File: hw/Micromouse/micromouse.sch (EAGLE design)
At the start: 57 parts, among them IC1 DSPIC33FJ64MC804-PT, IC2 DRV8833PWR, J1 GP2Y0A51SK0F, J2 GP2Y0A51SK0F, J3 GP2Y0A41SK0F, SW1 B3F-1000

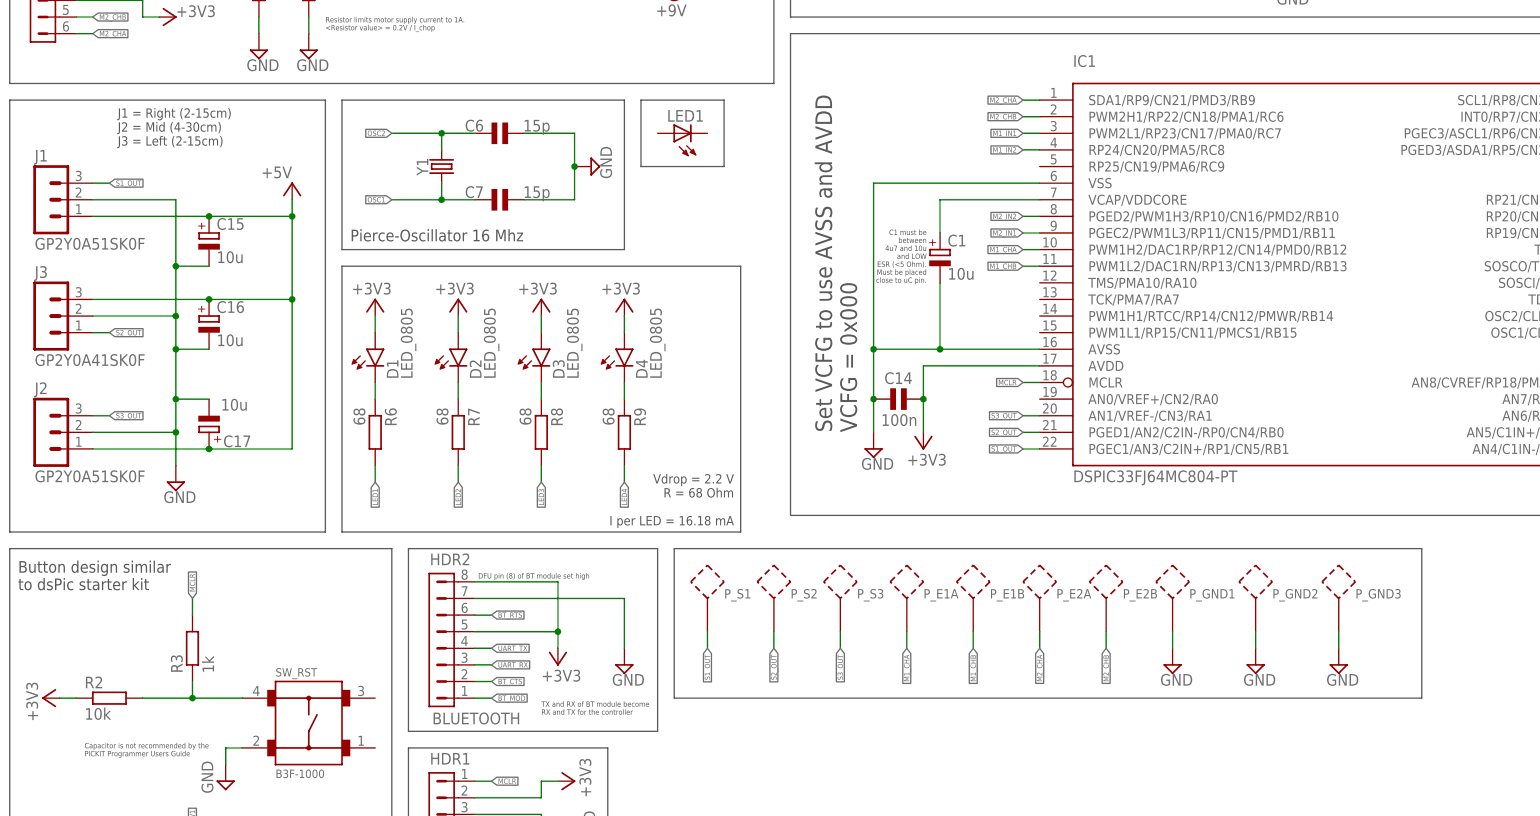
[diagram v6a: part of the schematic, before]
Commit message: Changes to the board according to design review
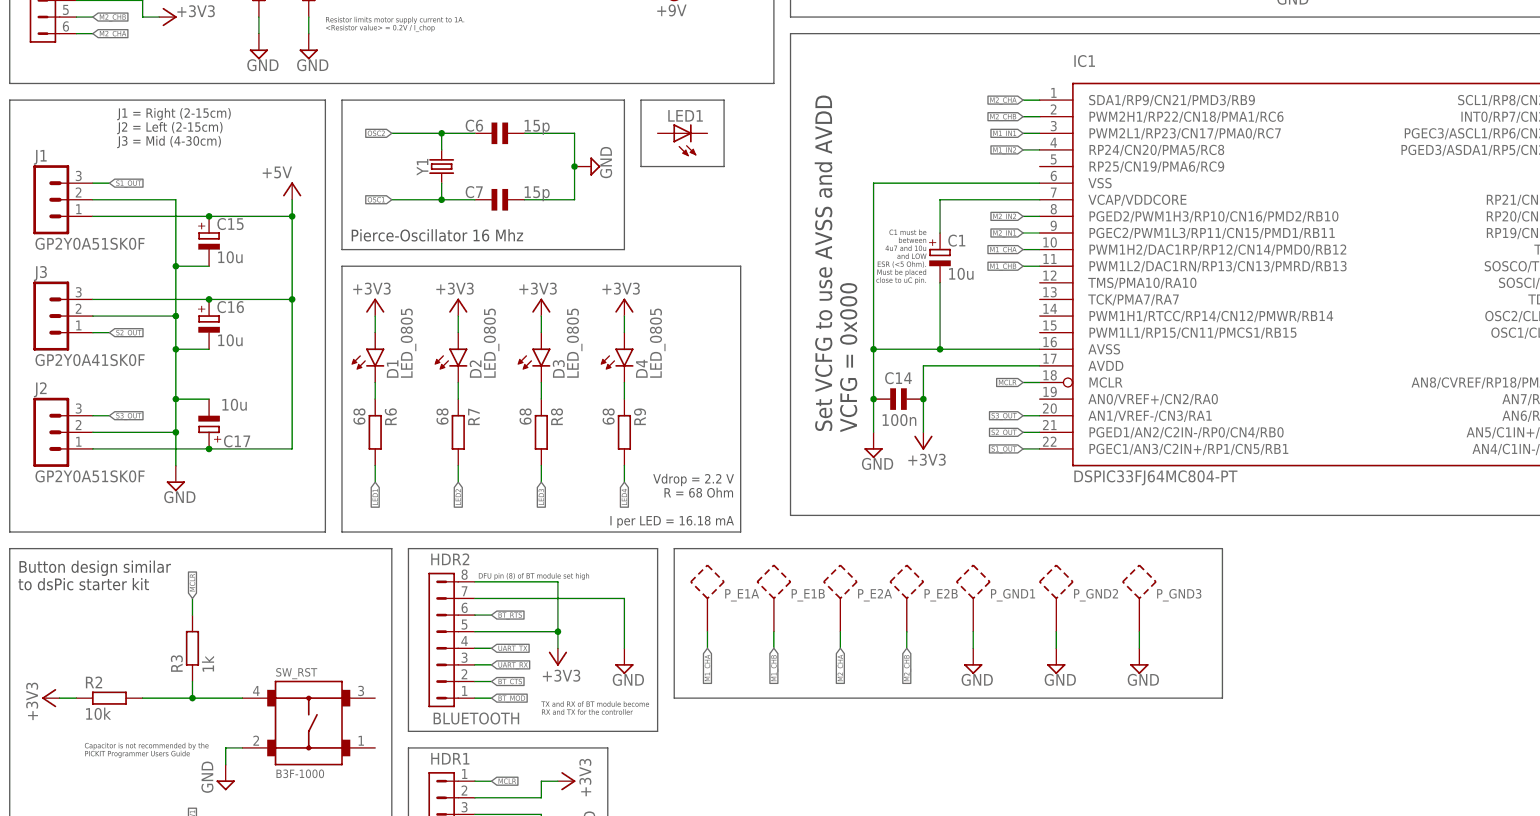
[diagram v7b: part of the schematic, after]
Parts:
- removed P_S1, P_S2, P_S3: (no value), micromouse:PROBE_POINTSMD
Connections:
- net S1_OUT: no longer P_S1.P$1
- net S2_OUT: no longer P_S2.P$1
- net S3_OUT: no longer P_S3.P$1
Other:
- note added: "J1 = Right (2-15cm) J2 = Left (2-15cm) J3 = Mid (4-30cm)"
- note removed: "J1 = Right (2-15cm) J2 = Mid (4-30cm) J3 = Left (2-15cm)"
- moved on the sheet: P_E1A, P_E1B, P_E2A, P_E2B, P_GND1, P_GND2, P_GND3

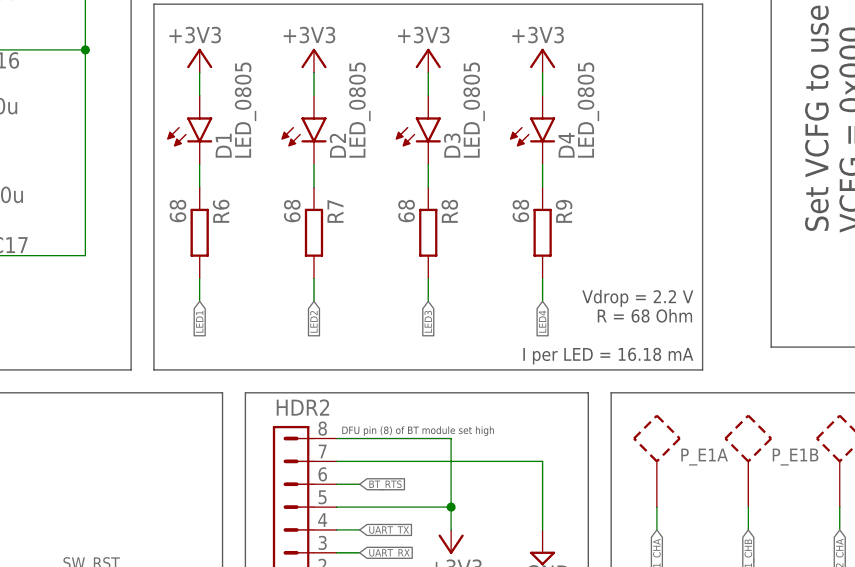
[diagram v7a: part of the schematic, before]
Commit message: Changed resistor values for LEDS
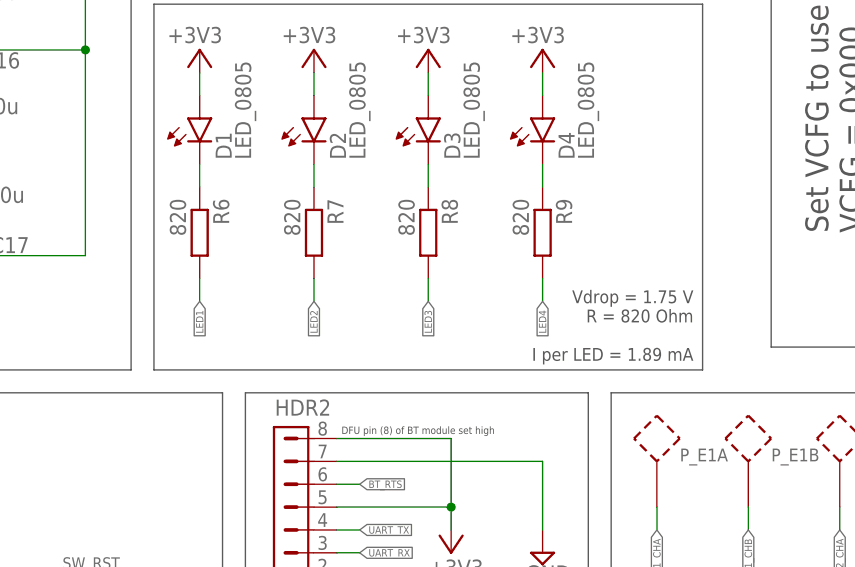
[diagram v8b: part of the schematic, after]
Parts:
- R6, R7, R8, R9: value 68 -> 820
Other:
- note added: "Vdrop = 1.75 V R = 820 Ohm I per LED = 1.89 mA"
- note removed: "Vdrop = 2.2 V R = 68 Ohm I per LED = 16.18 mA"
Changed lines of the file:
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@@
 <part name="R4" library="micromouse" library_urn="urn:adsk.eagle:library:26475156" deviceset="R_0805" device="" package3d_urn="urn:adsk.eagle:package:26475190/6" value="10k"/>
 <part name="R5" library="micromouse" library_urn="urn:adsk.eagle:library:26475156" deviceset="R_0805" device="" package3d_urn="urn:adsk.eagle:package:26475190/6" value="1k"/>
-<part name="R6" library="micromouse" library_urn="urn:adsk.eagle:library:26475156" deviceset="R_0805" device="" package3d_urn="urn:adsk.eagle:package:26475190/6" value="68"/>
-<part name="R7" library="micromouse" library_urn="urn:adsk.eagle:library:26475156" deviceset="R_0805" device="" package3d_urn="urn:adsk.eagle:package:26475190/6" value="68"/>
-<part name="R8" library="micromouse" library_urn="urn:adsk.eagle:library:26475156" deviceset="R_0805" device="" package3d_urn="urn:adsk.eagle:package:26475190/6" value="68"/>
-<part name="R9" library="micromouse" library_urn="urn:adsk.eagle:library:26475156" deviceset="R_0805" device="" package3d_urn="urn:adsk.eagle:package:26475190/6" value="68"/>
+<part name="R6" library="micromouse" library_urn="urn:adsk.eagle:library:26475156" deviceset="R_0805" device="" package3d_urn="urn:adsk.eagle:package:26475190/6" value="820"/>
+<part name="R7" library="micromouse" library_urn="urn:adsk.eagle:library:26475156" deviceset="R_0805" device="" package3d_urn="urn:adsk.eagle:package:26475190/6" value="820"/>
+<part name="R8" library="micromouse" library_urn="urn:adsk.eagle:library:26475156" deviceset="R_0805" device="" package3d_urn="urn:adsk.eagle:package:26475190/6" value="820"/>
+<part name="R9" library="micromouse" library_urn="urn:adsk.eagle:library:26475156" deviceset="R_0805" device="" package3d_urn="urn:adsk.eagle:package:26475190/6" value="820"/>
 <part name="HDR1" library="micromouse" library_urn="urn:adsk.eagle:library:26475156" deviceset="PICKIT_CON" device="" package3d_urn="urn:adsk.eagle:package:26475179/2"/>
 <part name="SUPPLY18" library="supply2" library_urn="urn:adsk.eagle:library:372" deviceset="GND" device=""/>
@@
 <text x="-55.372" y="72.644" size="0.8128" layer="97" align="top-left">C9 and C8 need to
 be low ESR ceramic</text>
-<text x="-34.036" y="-19.304" size="1.4224" layer="97" align="bottom-right">Vdrop = 2.2 V
-R = 68 Ohm
-I per LED = 16.18 mA</text>
+<text x="-34.036" y="-19.304" size="1.4224" layer="97" align="bottom-right">Vdrop = 1.75 V
+R = 820 Ohm
+I per LED = 1.89 mA</text>
 </plain>
 <instances>
